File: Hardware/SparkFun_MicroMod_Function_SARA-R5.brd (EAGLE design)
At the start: 37.5 x 65 mm, 119 parts, among them IC2 SN74AVC4T774PW, J1 MICROMOD_FUNCTION_STANDARD, J2 U.FL, J4 U.FL, J9 NANO_SIM, Q2 310mA/60V/1.6Ω, Q3 310mA/60V/1.6Ω, Q5 310mA/60V/1.6Ω, Q6 310mA/60V/1.6Ω, U1 SARA-R510M8S, U11 74HC1G04, U3 3.3V, U4 EEPROM, U8 AP7361C-33FGE

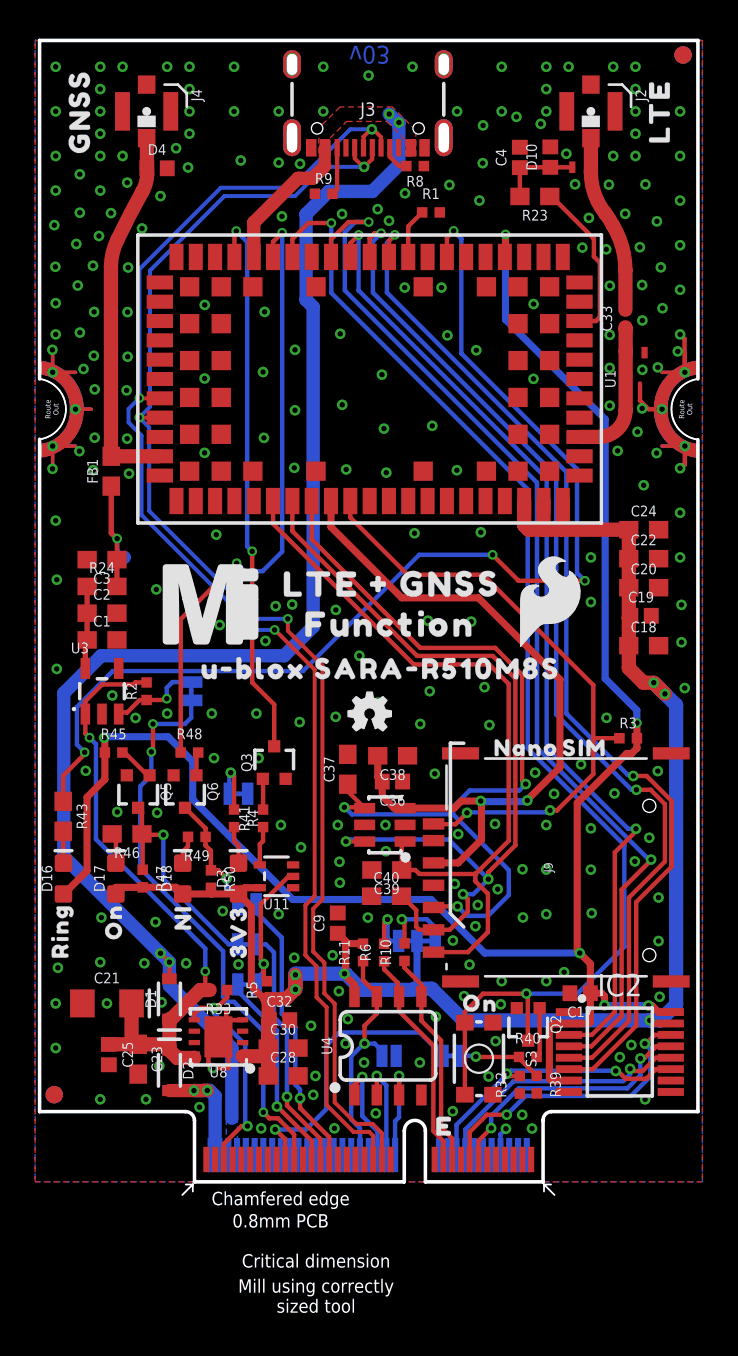
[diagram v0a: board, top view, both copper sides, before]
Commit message: pre-review changes (part 1)
-renamed all jumpers to match silk
-replaced I2C pullups to 2.2K
-Schematic Cleanup
-silk lines between tight passives in a row
-fixed acid trap off of pad 12
-tweaked via position near GND pad 14 to allow for flow
-routed GND to connect inner and perimeter GND pads on module.
-nudging of vias and traces to improve some gnd pour flow
-added mini VCC polygon over m.2 connector pads for better flow
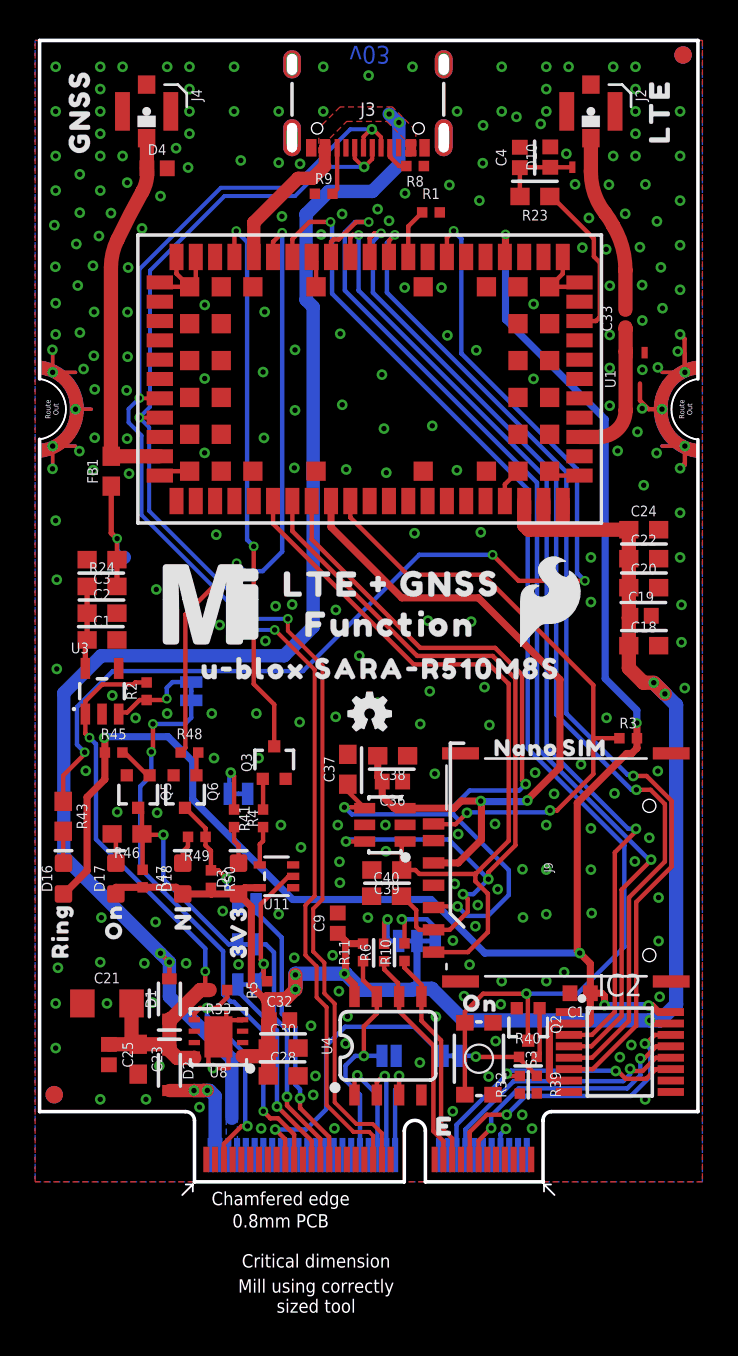
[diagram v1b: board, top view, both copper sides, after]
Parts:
- removed U$50: (no value), output:#I2C_PULLUP#5
- added U$4: (no value), output:#3V3_LED#0
- R10, R6: value 4.7k -> 2.2k
- U$1: device output:#3#3V_LED#0 -> output:#I2C#0
- moved LOGO3 34.7 mm to (45.7, 58.4)
- moved U$1 8.52 mm to (18.5, 13.7)
- moved FRAME2 3.81 mm to (3.81, -17.8)
- renumbered JP1 to 3V3_LED, JP2 to I2C, JP3 to WP, JP4 to ANT_REG_EN, JP5 to LTE_PWR_ON, JP6 to LTE_NI, JP7 to LTE_ON, JP8 to LTE_RESET
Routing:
- net GND: track 19.0 -> 35.9 mm, vias 261 -> 260
- added copper zone on layer 16, net VCC
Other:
- board text added: "0.8mm PCB ENIG Finish 45 degree chamfered edge 2-layer Board Soldermask Color: red"
- board text removed: "0.8mm PCB ENIG Finish 45 degree chamfered edge"

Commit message: Moved VCCIO away from LTE_ANT
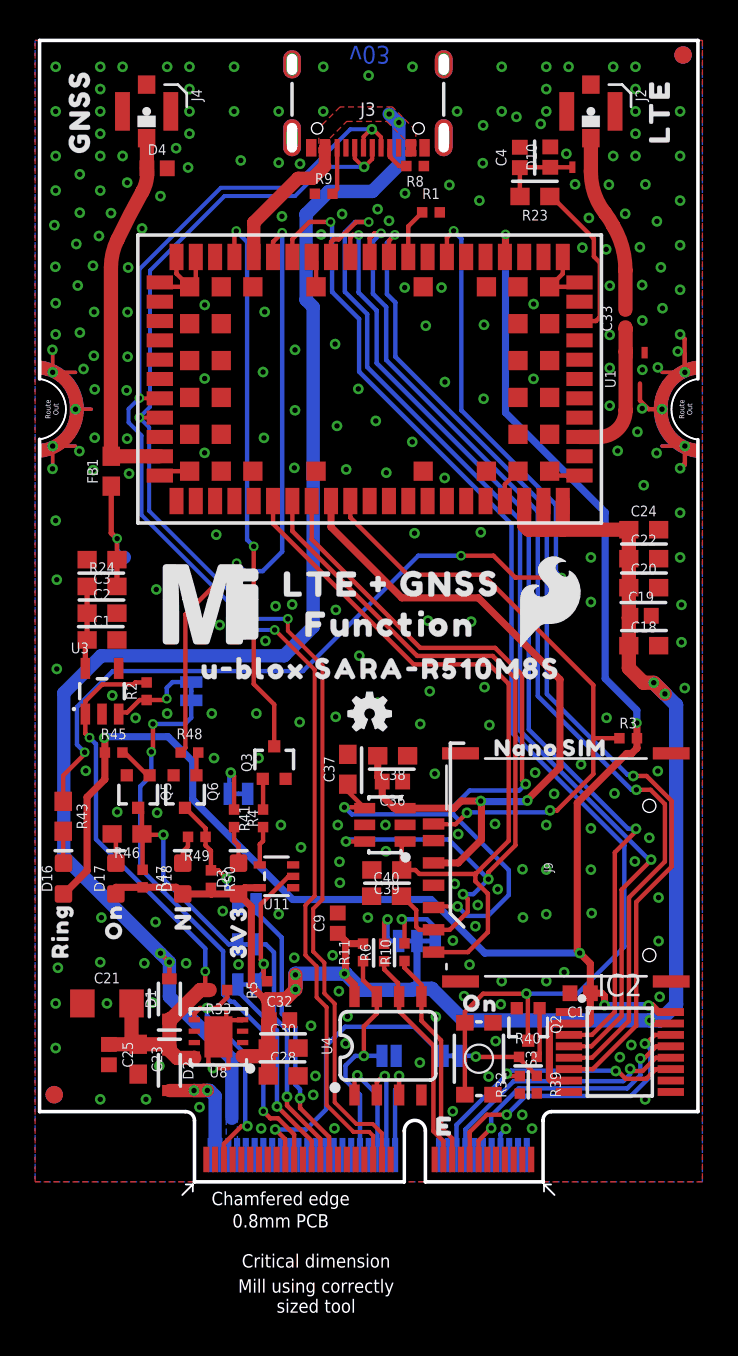
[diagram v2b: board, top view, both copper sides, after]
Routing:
- net LTE_18_RI: track 63.9 -> 61.7 mm
- net GND: vias 260 -> 262

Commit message: USB_SHLD jumper added
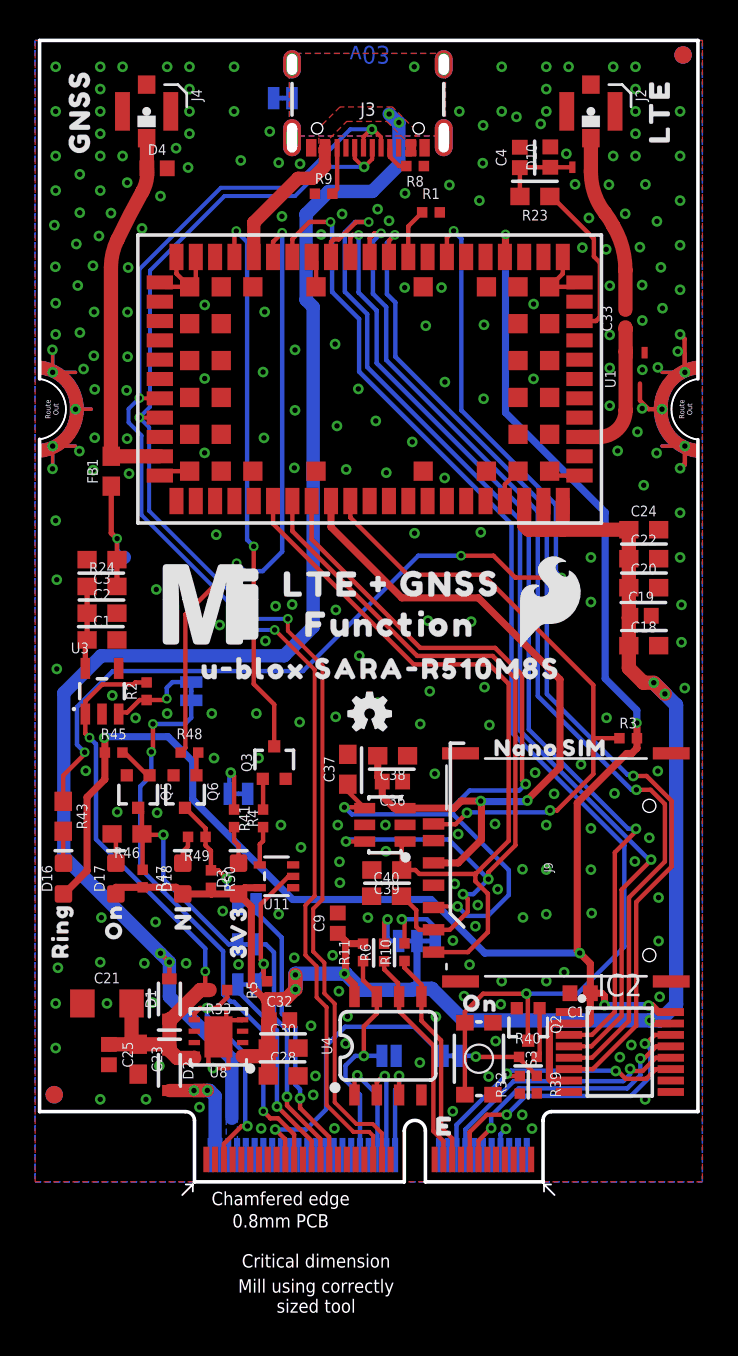
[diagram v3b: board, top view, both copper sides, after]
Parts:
- added U$21: (no value), output:#USB_SHLD#0
- added USB_SHLD: JUMPER-SMT_2_NC_TRACE_SILK, SparkFun-Jumpers:SMT-JUMPER_2_NC_TRACE_SILK
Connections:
- new net SHLD: J3.SHLD1, J3.SHLD2, J3.SHLD3, J3.SHLD4, USB_SHLD.1
- net GND: now also USB_SHLD.2; no longer J3.SHLD1, J3.SHLD2, J3.SHLD3, J3.SHLD4
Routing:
- net GND: vias 262 -> 258
- added copper zone on layer 1, net SHLD
- added copper zone on layer 16, net SHLD
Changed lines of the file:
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@@
 <setting verticaltext="up"/>
 </settings>
-<grid distance="0.05" unitdist="inch" unit="inch" style="lines" multiple="1" display="yes" altdistance="0.0001" altunitdist="inch" altunit="inch"/>
+<grid distance="0.05" unitdist="inch" unit="inch" style="lines" multiple="1" display="yes" altdistance="0.005" altunitdist="inch" altunit="inch"/>
 <layers>
 <layer number="1" name="Top" color="4" fill="1" visible="yes" active="yes"/>
@@
 <layer number="98" name="Guide" color="6" fill="1" visible="no" active="no"/>
 <layer number="99" name="SpiceOrder" color="7" fill="1" visible="no" active="no"/>
-<layer number="100" name="Muster" color="7" fill="1" visible="no" active="yes"/>
+<layer number="100" name="Muster" color="7" fill="1" visible="yes" active="yes"/>
 <layer number="101" name="Patch_Top" color="12" fill="4" visible="no" active="no"/>
 <layer number="102" name="Vscore" color="7" fill="1" visible="no" active="no"/>
@@
 <element name="U$4" library="output" package="#3V3_LED#0" value="" x="16.637" y="22.098" smashed="yes" rot="MR0"/>
 <element name="U$1" library="output" package="#I2C#0" value="" x="18.542" y="13.716" smashed="yes" rot="MR0"/>
+<element name="USB_SHLD" library="SparkFun-Jumpers" package="SMT-JUMPER_2_NC_TRACE_SILK" package3d_urn="urn:adsk.eagle:package:39281/1" value="JUMPER-SMT_2_NC_TRACE_SILK" x="14.10461875" y="61.714378125" smashed="yes" rot="MR0">
+<attribute name="NAME" x="14.10461875" y="62.857378125" size="0.6096" layer="26" font="vector" ratio="20" rot="MR0" align="bottom-center"/>
+<attribute name="VALUE" x="14.10461875" y="60.571378125" size="0.6096" layer="28" font="vector" ratio="20" rot="MR0" align="top-center"/>
+</element>
+<element name="U$21" library="output" package="#USB_SHLD#0" value="" x="19.5453" y="61.724540625" smashed="yes" rot="MR0"/>
 </elements>
 <signals>
@@
 <contactref element="J1" pad="GND6"/>
 <contactref element="3V3_LED" pad="1"/>
-<contactref element="J3" pad="GND2"/>
-<contactref element="J3" pad="GND"/>
 <contactref element="R9" pad="1"/>
-<polygon width="0.2032" layer="1" isolate="0.1778" rank="2">
+<polygon width="0.2032" layer="1" isolate="0.1778" rank="3">
 <vertex x="38" y="0"/>
 <vertex x="0" y="0"/>
@@
 <vertex x="0" y="65"/>
 </polygon>
-<contactref element="J3" pad="SHLD2"/>
-<contactref element="J3" pad="SHLD3"/>
-<contactref element="J3" pad="SHLD1"/>
-<contactref element="J3" pad="SHLD4"/>
 <contactref element="R8" pad="1"/>
 <contactref element="U4" pad="4"/>
@@
 <via x="11.33" y="60.96" extent="1-16" drill="0.3048" diameter="0.6096"/>
 <via x="11.33" y="63.5" extent="1-16" drill="0.3048" diameter="0.6096"/>
-<via x="13.87" y="60.96" extent="1-16" drill="0.3048" diameter="0.6096"/>
-<via x="16.41" y="63.5" extent="1-16" drill="0.3048" diameter="0.6096"/>
-<via x="16.41" y="60.96" extent="1-16" drill="0.3048" diameter="0.6096"/>
-<via x="18.9906375" y="63.002159375" extent="1-16" drill="0.3048" diameter="0.6096"/>
-<via x="21.49" y="63.5" extent="1-16" drill="0.3048" diameter="0.6096"/>
-<via x="24.03" y="60.96" extent="1-16" drill="0.3048" diameter="0.6096"/>
+<via x="13.362" y="59.817" extent="1-16" drill="0.3048" diameter="0.6096"/>
+<via x="24.157" y="60.96" extent="1-16" drill="0.3048" diameter="0.6096"/>
 <via x="30.253" y="58.547" extent="1-16" drill="0.3048" diameter="0.6096"/>
 <via x="26.57" y="63.5" extent="1-16" drill="0.3048" diameter="0.6096"/>
@@
 <via x="23.3340375" y="45.547278125" extent="1-16" drill="0.3048" diameter="0.6096"/>
 <via x="25.538759375" y="44.594778125" extent="1-16" drill="0.3048" diameter="0.6096"/>
+<contactref element="J3" pad="GND2"/>
+<contactref element="J3" pad="GND"/>
+<contactref element="USB_SHLD" pad="2"/>
+<polygon width="0.2032" layer="16" isolate="0.2032" rank="2">
+<vertex x="0" y="0"/>
+<vertex x="38" y="0"/>
+<vertex x="38" y="65"/>
+<vertex x="0" y="65"/>
+</polygon>
 </signal>
 <signal name="EN">
@@
 <wire x1="30.590875" y1="57.776496875" x2="30.5943" y2="57.779921875" width="0.254" layer="1"/>
 </signal>
+<signal name="SHLD">
+<contactref element="J3" pad="SHLD3"/>
+<contactref element="J3" pad="SHLD1"/>
+<contactref element="J3" pad="SHLD4"/>
+<contactref element="J3" pad="SHLD2"/>
+<contactref element="USB_SHLD" pad="1"/>
+<polygon width="0.2032" layer="1" isolate="0.3048" rank="2">
+<vertex x="14.478" y="64.262"/>
+<vertex x="14.478" y="59.563"/>
+<vertex x="23.368" y="59.563"/>
+<vertex x="23.368" y="64.262"/>
+</polygon>
+<via x="21.59" y="63.5" extent="1-16" drill="0.3048" diameter="0.6096"/>
+<polygon width="0.2032" layer="16" isolate="0.3048">
+<vertex x="14.478" y="64.262"/>
+<vertex x="14.478" y="59.563"/>
+<vertex x="23.368" y="59.563"/>
+<vertex x="23.368" y="64.262"/>
+</polygon>
+</signal>
 </signals>

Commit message: Sim connector re-routing
-IC2 ref to U2
-Updated Nano SIM FP to have tRestrict area underneath
-moved traces under the SIM connector to bottom layer
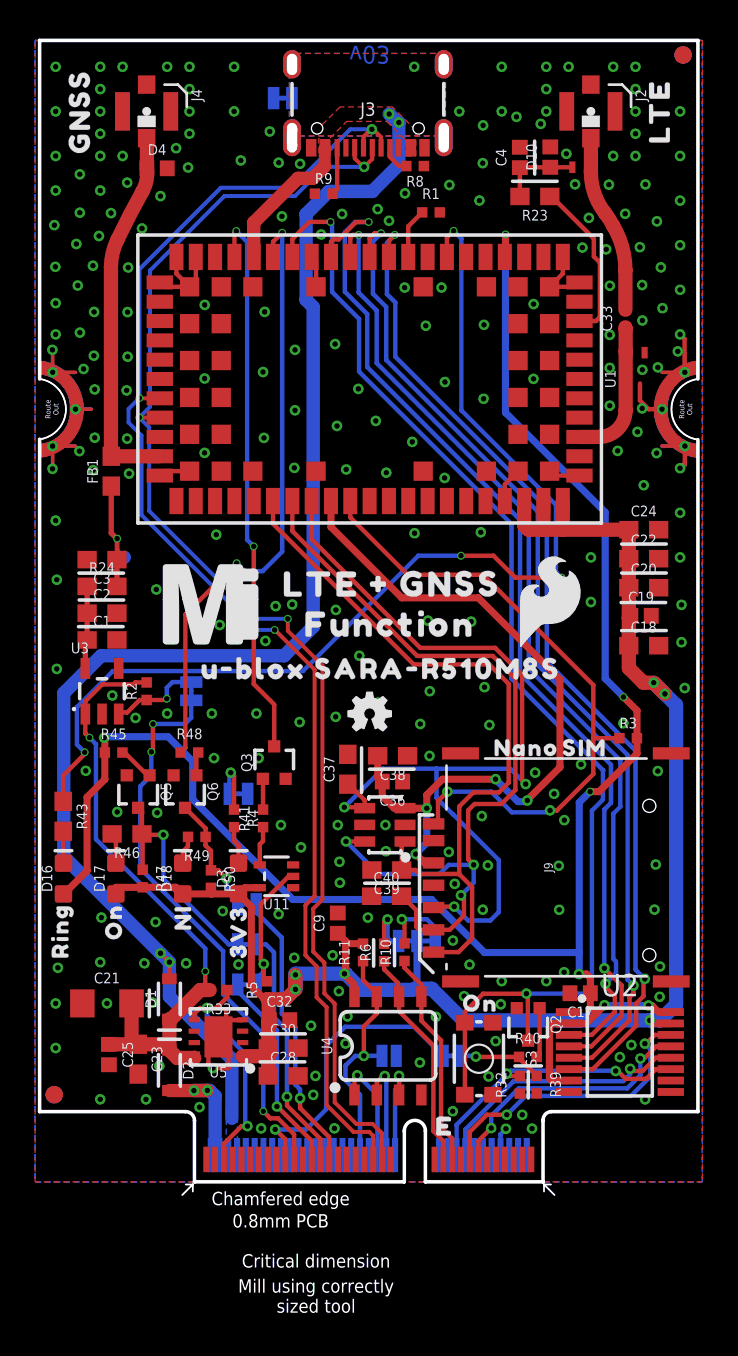
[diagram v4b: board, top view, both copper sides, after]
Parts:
- renumbered IC2 to U2, U8 to U5
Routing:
- net SIM_RST: track 49.0 -> 52.1 mm
- net LTE_18_CTS: track 59.5 -> 57.4 mm
- net LTE_18_RTS: track 59.6 -> 57.8 mm
- net SIM_DET: track 35.6 -> 37.2 mm
- net LTE_18_RXO: track 61.4 -> 60.3 mm
- net LTE_18_PWR_ON: track 69.9 -> 69.2 mm
- net VCCIO: track 106.4 -> 106.1 mm, vias 6 -> 7
- net VSIM: track 42.4 -> 42.5 mm, vias 2 -> 4
- net GND: vias 258 -> 250
- added copper zone on layer 15, net 3.3V
- added copper zone on layer 2, net GND

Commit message: More changes from group review
-Now it's a 4-layer, removed some 3.3V traces from bottom copper, added vias as necessary to connect to 3.3V inner layer.
-Changed where regulators (U3 and U5) enable pins are tied up to. They are now tied up to the 3.3V provided by the MM Main board. Previously, they were connected to VIN, which could be higher than 3.3V and damage enable control GPIO on some processor boards.
-Disconnected V_USB from MM m.2 connector.
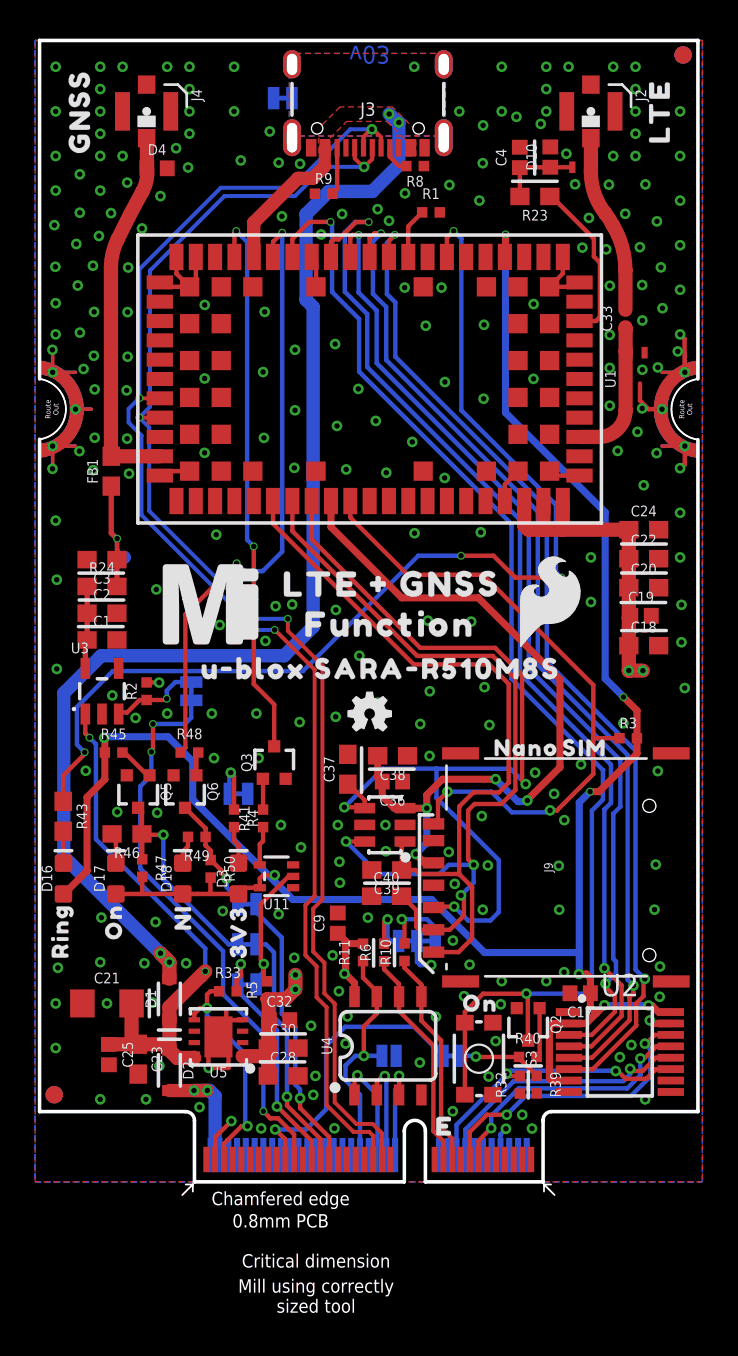
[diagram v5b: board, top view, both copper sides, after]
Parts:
- moved R47 0.60 mm to (6.10, 17.9)
- moved R50 0.58 mm to (10.00, 17.8)
- moved R33 0.54 mm to (11.0, 10.9), turned to 0 degrees
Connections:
- new net 3.3V_IN: J1.73, R2.2, R33.2
- net VIN: no longer R2.2, R33.2
- net V_USB: no longer J1.70
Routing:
- net 3.3V: track 99.3 -> 49.9 mm, vias 6 -> 8
- net 3.3V_IN: track 0.00 -> 32.7 mm, vias 0 -> 3
- net V_USB: track 87.3 -> 76.9 mm
- net VIN: track 36.0 -> 30.7 mm
- net LTE_!ON!: track 13.2 -> 12.6 mm
- net GND: track 35.9 -> 36.0 mm, vias 250 -> 249
- removed copper zone on layer 16, net V_USB
